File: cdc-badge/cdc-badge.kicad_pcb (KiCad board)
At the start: 4 copper layers, 85 x 110 mm, 158 parts, among them J1 USB_C, J2 JST S2B-PH-SM4-TB, J3 Conn_02x20_Odd_Even, J4 Conn_Grove, J5 Conn_02x03_Odd_Even, J6 Conn_01x06, J7 Conn_01x24, Q1 Si1308EDL, Q2 Si1308EDL, SW0 0, SW1 1, SW10 YES, SW11 NO, SW12 power on/reset, SW13 reset, SW14 flash/power off, SW15 MST-22D18G2 3J, SW16 MST-22D18G2 3J, SW17 MS-22D28-G020, SW2 2, SW3 3, SW4 4, SW5 5, SW6 6, SW7 7, SW8 8, SW9 9, U1 ESP32-S3-WROOM-1-N16R8, U2 TCA9535PWR, U3 TR01-C2P-T301, U5 TLV61070ADBVR, U6 BQ25895RTW, U7 USBLC6-2SC6, U8 TLV62569DBV

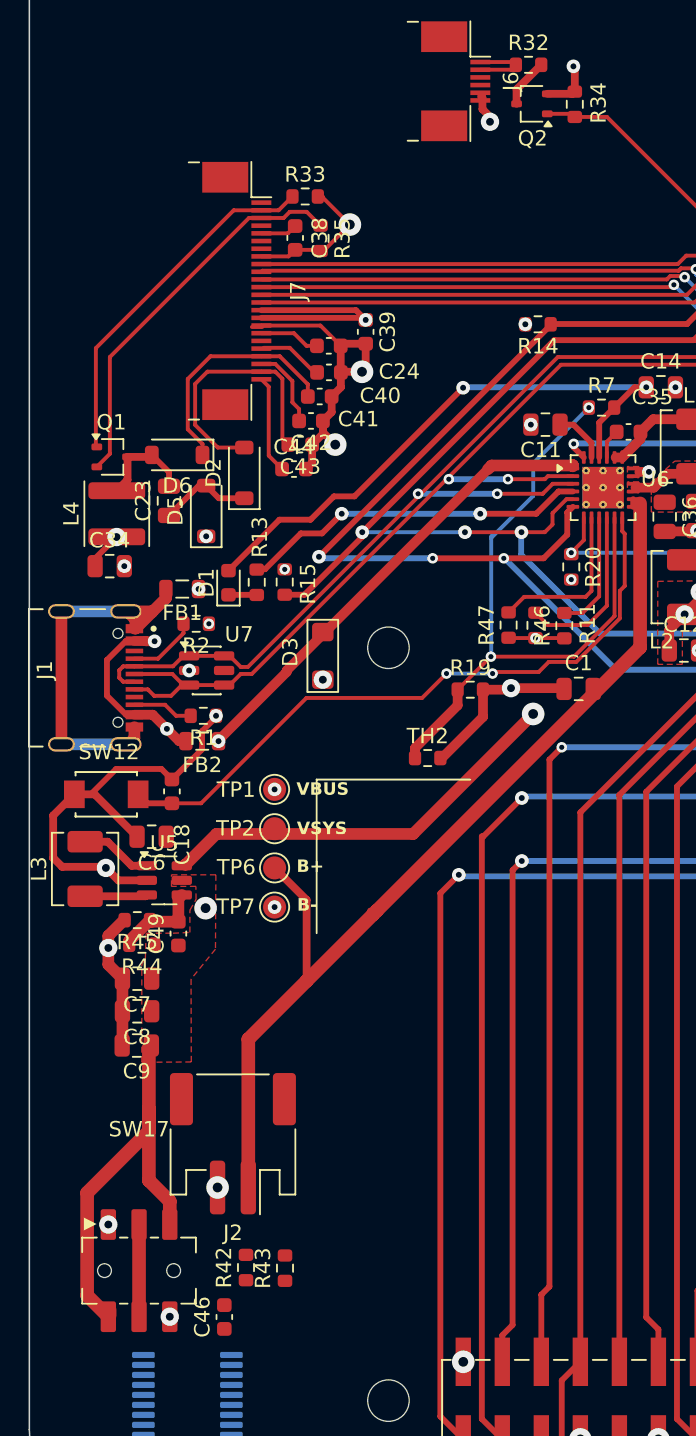
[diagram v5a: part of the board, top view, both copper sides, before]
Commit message: PCB: Reviewed wirings, fixed some errors
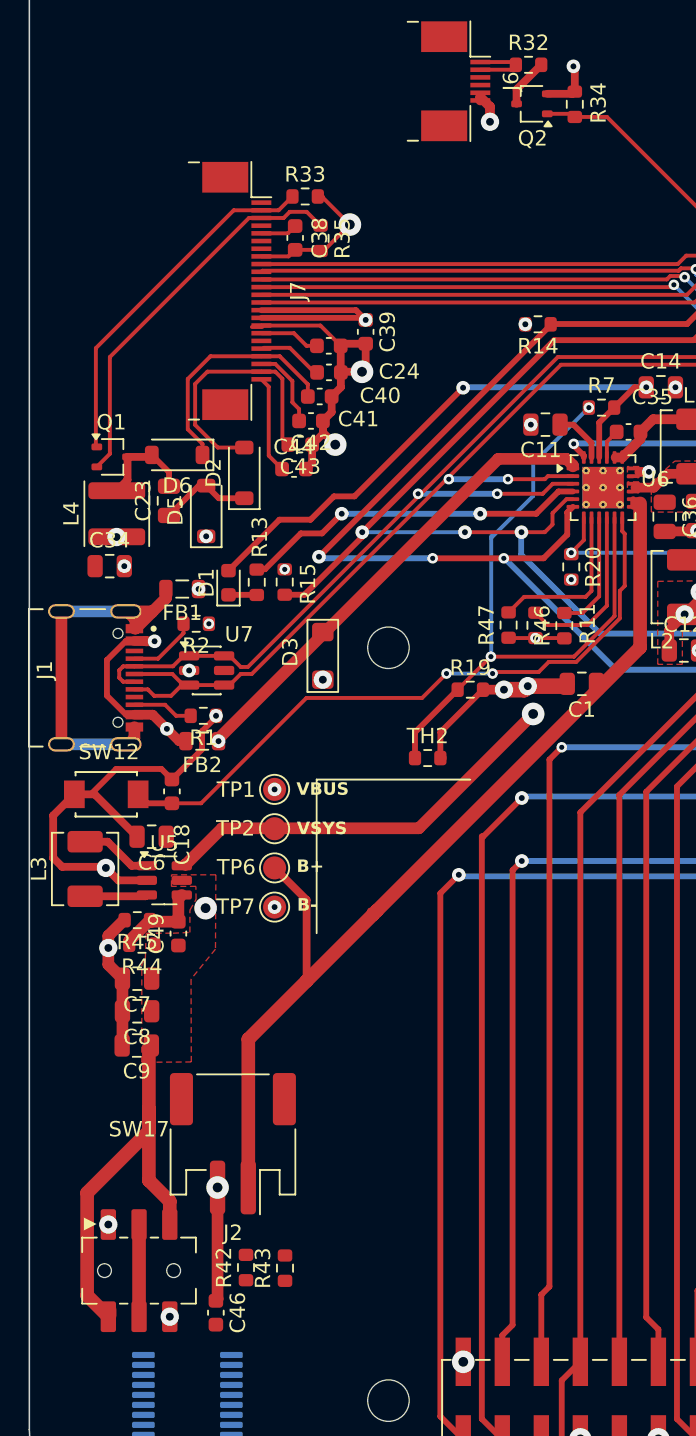
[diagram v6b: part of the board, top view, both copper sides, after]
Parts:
- moved C46 0.62 mm to (35.9, 138.9), turned to -90 degrees
- moved C1 0.39 mm to (59.7, 98.0), turned to 180 degrees
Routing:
- net GND: track 146.4 -> 154.2 mm, vias 44 -> 45
- net +3.3V: track 44.4 -> 43.0 mm

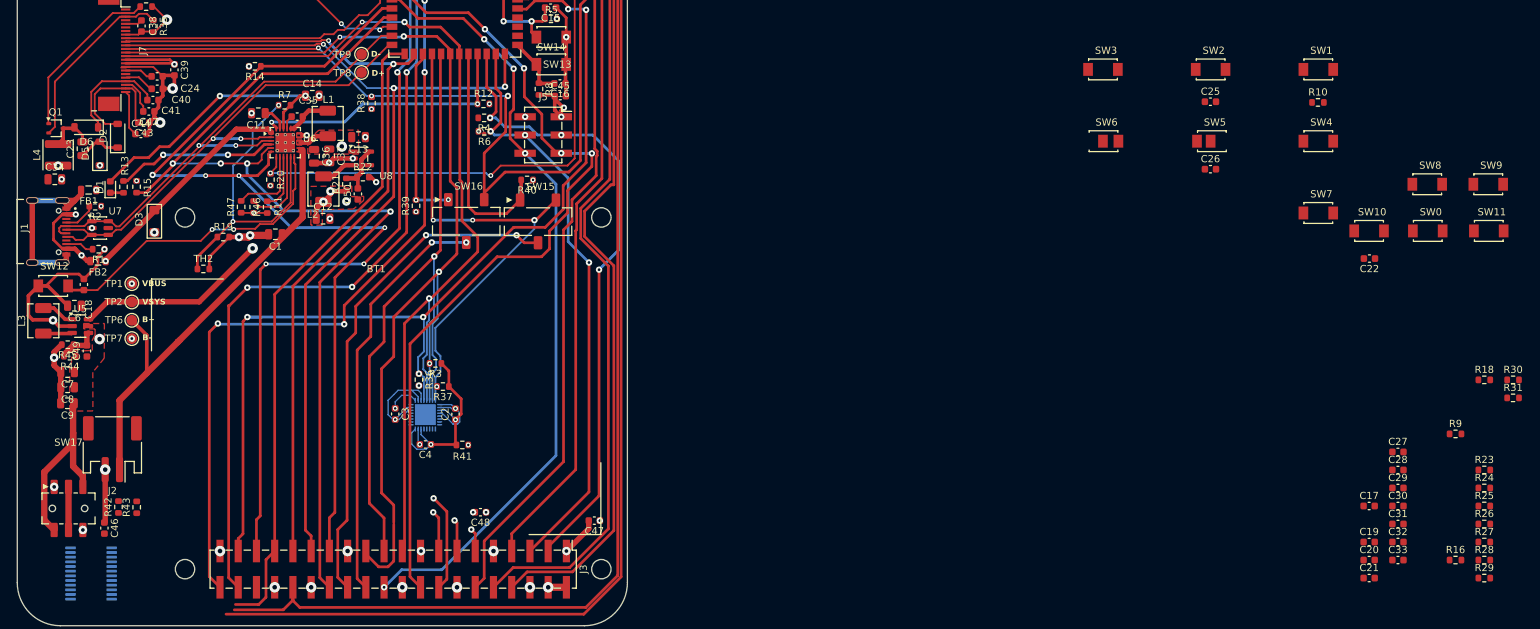
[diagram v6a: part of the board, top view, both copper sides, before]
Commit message: PCB: placement and begin routing for the buttons/keypad
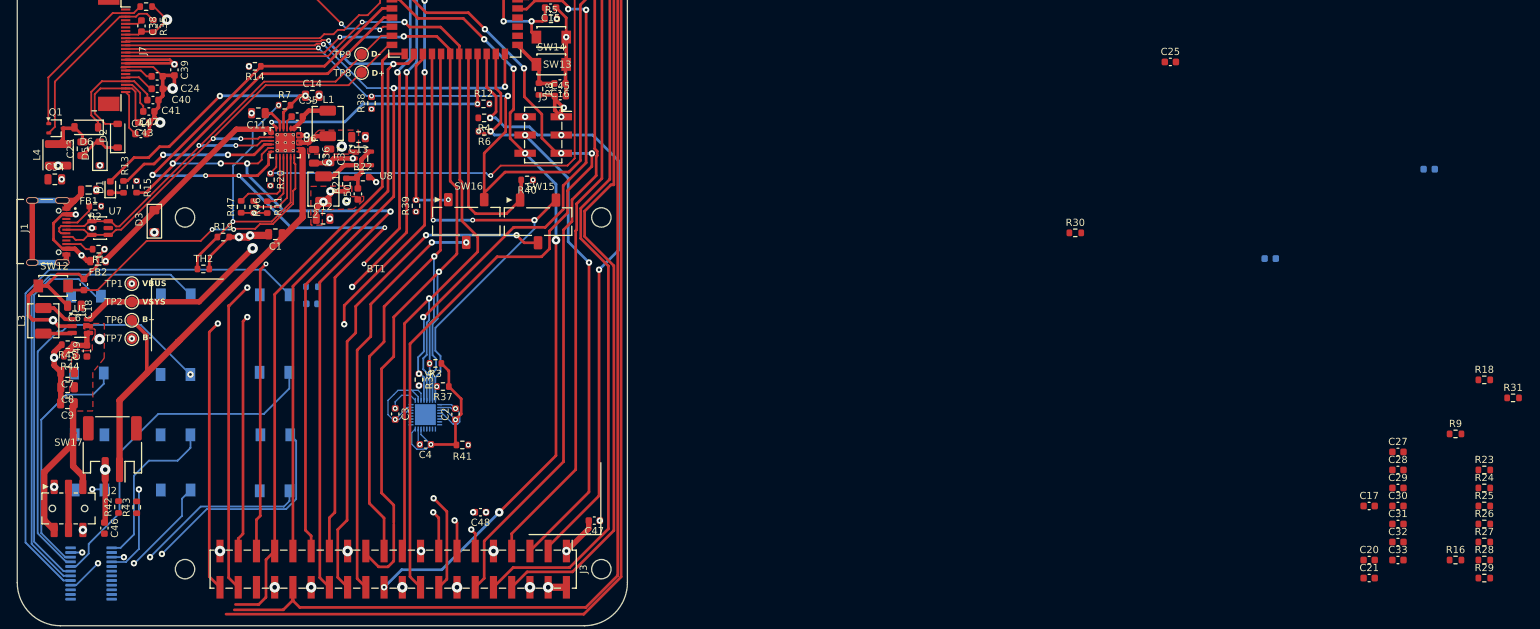
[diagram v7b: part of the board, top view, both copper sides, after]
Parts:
- C19, C22, C26, R10, SW0, SW1, SW10, SW11, SW2, SW3, SW4, SW5, SW6, SW7, SW8, SW9: moved to B.Cu
- moved SW11 198.2 mm to (33.8, 133.6), turned to 180 degrees
- moved SW9 198.0 mm to (33.8, 125.9), turned to 180 degrees
- moved SW0 178.1 mm to (45.8, 133.6), turned to 180 degrees
- moved SW8 177.8 mm to (45.8, 125.9), turned to 180 degrees
- moved SW10 156.7 mm to (59.6, 133.7), turned to 180 degrees
- moved C19 151.0 mm to (64.8, 107.7), turned to 180 degrees
- moved SW4 148.9 mm to (59.6, 117.2), turned to 180 degrees
- moved SW1 148.7 mm to (59.6, 106.4), turned to 180 degrees
- moved SW7 148.5 mm to (59.7, 125.9), turned to 180 degrees
- moved SW5 148.0 mm to (45.8, 117.5), turned to 180 degrees
- moved SW2 147.5 mm to (45.8, 106.4), turned to 180 degrees
- moved SW3 145.2 mm to (33.3, 106.6), turned to 180 degrees
- moved SW6 145.0 mm to (33.7, 117.3), turned to 180 degrees
- moved R10 142.5 mm to (64.8, 105.3), turned to 180 degrees
- moved R30 64.3 mm to (171.1, 97.8)
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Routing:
- net /BTN_1: track 0.00 -> 82.8 mm
- net /BTN_2: track 0.00 -> 66.5 mm
- net /BTN_5: track 0.00 -> 57.2 mm, vias 0 -> 1
- net /BTN_3: track 0.00 -> 52.4 mm
- net /BTN_4: track 0.00 -> 49.1 mm
- net /BTN_7: track 0.00 -> 44.7 mm, vias 0 -> 2
- net /BTN_6: track 0.00 -> 33.5 mm
- net /BTN_YES: track 0.00 -> 29.4 mm, vias 0 -> 2
- net /BTN_0: track 0.00 -> 23.6 mm, vias 0 -> 2
- net /BTN_8: track 0.00 -> 23.4 mm
- net /BTN_NO: track 0.00 -> 21.1 mm, vias 0 -> 2
- net /TR01_IRQ: track 137.7 -> 135.7 mm
- net /SAO_GPIO2: vias 4 -> 6

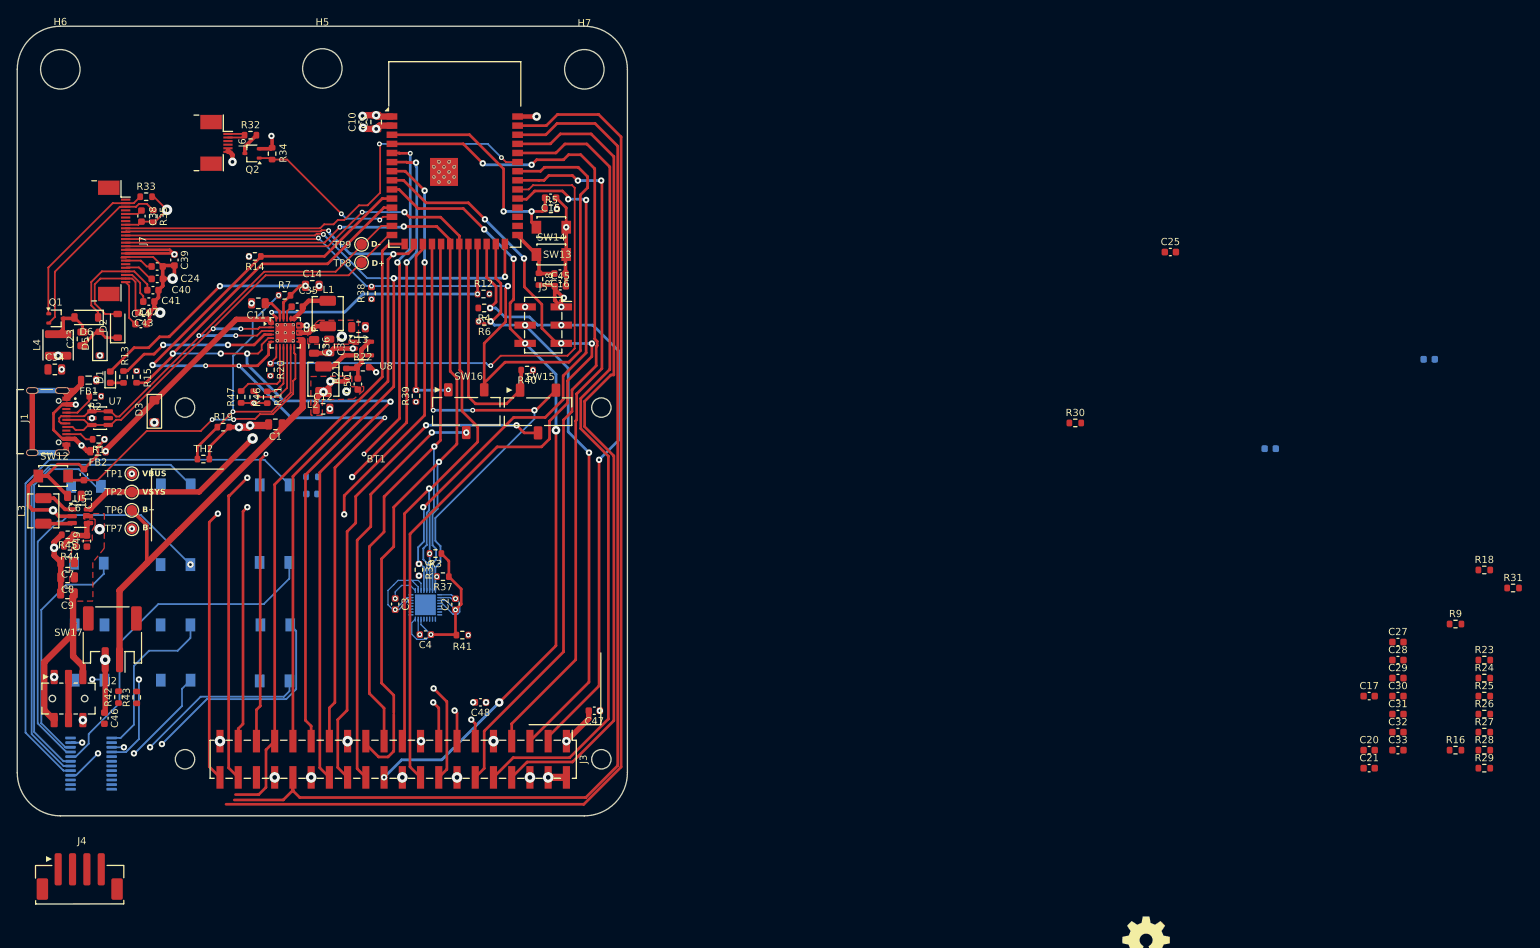
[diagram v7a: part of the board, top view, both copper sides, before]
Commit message: PCB: Erased all Components and tracks for full redesign
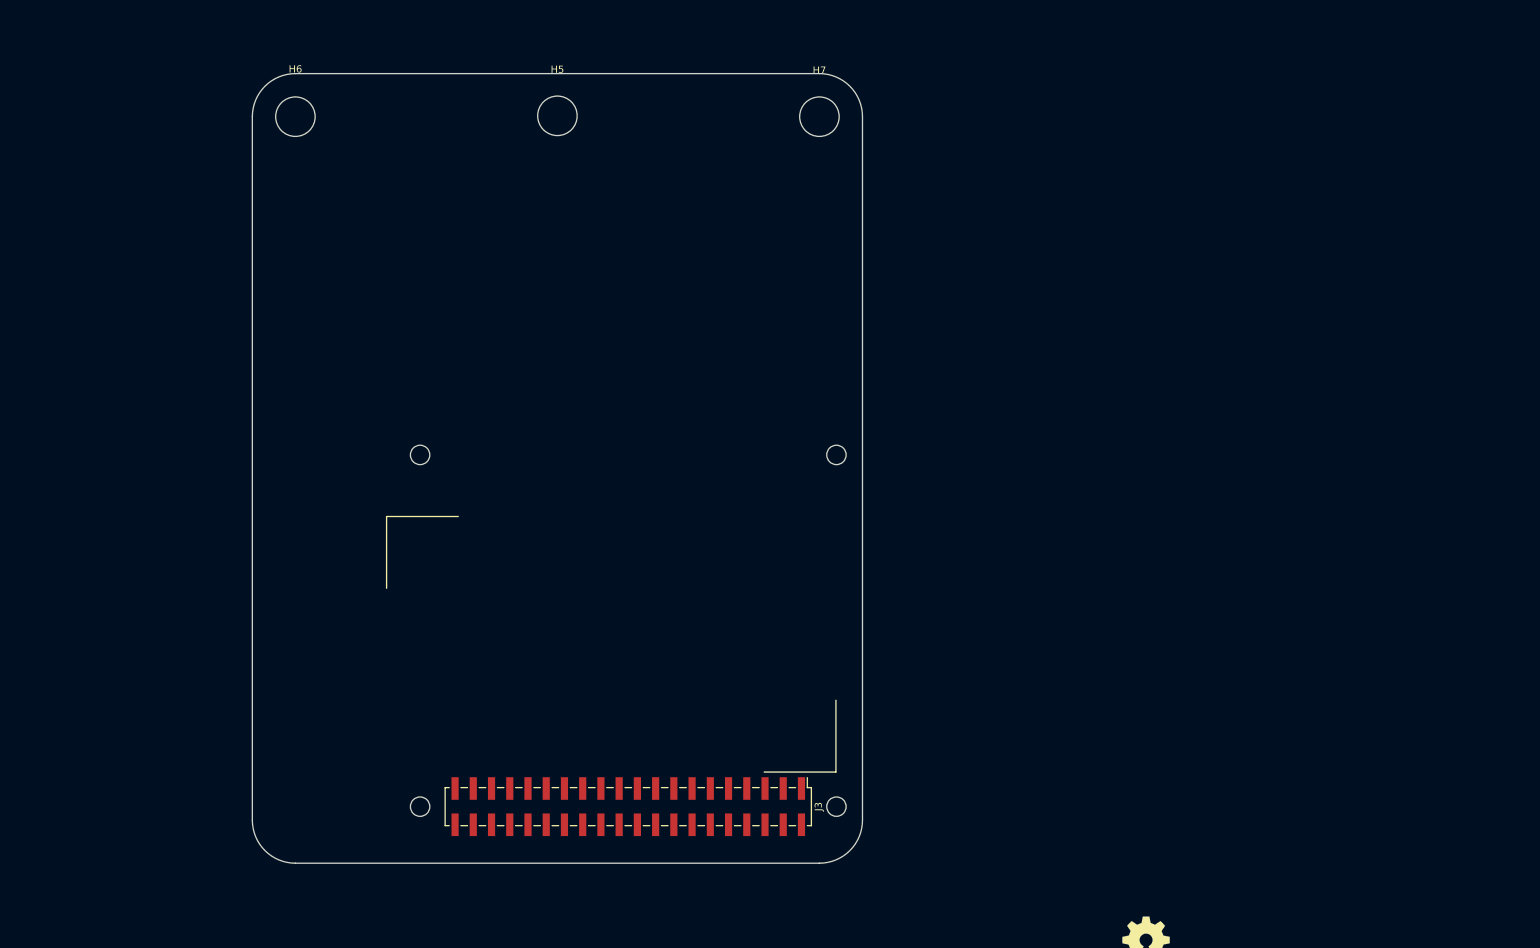
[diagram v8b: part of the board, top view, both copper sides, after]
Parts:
- removed C1, C11, C12, C36, C37, C5, C6, C7, C8, C9: 10uF, Capacitor_SMD:C_0805_2012Metric
- removed C10, C15, C16, C17, C18, C19, C2, C20, C21, C22, C25, C26, C27, C28, C29, C3, C30, C31, C32, C4: 100nF, Capacitor_SMD:C_0603_1608Metric
- removed C13, C14, C23, C34: 4.7uF, Capacitor_SMD:C_0805_2012Metric
- removed C24, C33, C38, C39, C40, C41, C42, C43, C44, C45, C46, C47, C48: 1uF, Capacitor_SMD:C_0603_1608Metric
- removed C35: 47nF, Capacitor_SMD:C_0603_1608Metric
- removed C49, C50: NA, Capacitor_SMD:C_0603_1608Metric
- removed D1: red, LED_SMD:LED_0603_1608Metric
- removed D2, D5, D6: MBR0530, Diode_SMD:D_SOD-123
- removed D3: SMF14CA, CDC_Badge:D_SOD-123FL_Unpolarized
- removed DS1: GDEY029T94-FL03, CDC_Badge:GDEY029T94-FL03
- removed FB1: 30Ω@100MHz, Inductor_SMD:L_0805_2012Metric
- removed FB2: 120Ω@100MHz, Inductor_SMD:L_0805_2012Metric
- removed J1: USB_C, CDC_Badge:SHOUHAN_TYPE-C_16PIN_2MD_073
- removed J2: JST S2B-PH-SM4-TB, Connector_JST:JST_PH_S2B-PH-SM4-TB_1x02-1MP_P2.00mm_Horizontal
- removed J4: Conn_Grove, CDC_Badge:BOOMELE_HY-4P_1x04-1MP_P2mm_Vertical
- removed J5: Conn_02x03_Odd_Even, Connector_PinSocket_2.54mm:PinSocket_2x03_P2.54mm_Vertical_SMD
- removed J6: Conn_01x06, Connector_FFC-FPC:Jushuo_AFC07-S06FCA-00_1x6-1MP_P0.50_Horizontal
- removed J7: Conn_01x24, Connector_FFC-FPC:Jushuo_AFC07-S24FCA-00_1x24-1MP_P0.50_Horizontal
- removed L1, L2, L3: 2.2uH, Inductor_SMD:L_TechFuse_SL0420
- removed L4: 47uH, Inductor_SMD:L_Changjiang_FNR4030S
- removed Q1, Q2: Si1308EDL, Package_TO_SOT_SMD:SOT-323_SC-70
- removed R1, R13, R2, R7: 5.1k, Resistor_SMD:R_0603_1608Metric
- removed R10, R16, R18, R23, R24, R25, R26, R27, R28, R29, R3, R30, R31, R36, R37, R38, R39, R40: 47k, Resistor_SMD:R_0603_1608Metric
- removed R11: 220, Resistor_SMD:R_0603_1608Metric
- removed R12, R14, R15, R20, R4, R42, R43, R46, R47, R5, R6, R8, R9, TH2: 10k, Resistor_SMD:R_0603_1608Metric
- removed R19, R22: 30k, Resistor_SMD:R_0603_1608Metric
- removed R21: 135k, Resistor_SMD:R_0603_1608Metric
- removed R32: 5.1, Resistor_SMD:R_0603_1608Metric
- removed R33, R34: 1M, Resistor_SMD:R_0603_1608Metric
- removed R35: 2.2, Resistor_SMD:R_0603_1608Metric
- removed R41: 0, Resistor_SMD:R_0603_1608Metric
- removed R44: 820k, Resistor_SMD:R_0603_1608Metric
- removed R45: 91k, Resistor_SMD:R_0603_1608Metric
- removed SW0: 0, CDC_Badge:TS-1088-AR02016
- removed SW1: 1, CDC_Badge:TS-1088-AR02016
- removed SW10: YES, CDC_Badge:TS-1088-AR02016
- removed SW11: NO, CDC_Badge:TS-1088-AR02016
- removed SW12: power on/reset, CDC_Badge:TS-1088-AR02016
- removed SW13: reset, CDC_Badge:TS-1088-AR02016
- removed SW14: flash/power off, CDC_Badge:TS-1088-AR02016
- removed SW15, SW16: MST-22D18G2 3J, CDC_Badge:SW_SPDT_Shouhan_MST-22D18G2_3J
- removed SW17: MS-22D28-G020, CDC_Badge:SW_DPDT_G-Switch_MS-22D28-G020
- removed SW2: 2, CDC_Badge:TS-1088-AR02016
- removed SW3: 3, CDC_Badge:TS-1088-AR02016
- removed SW4: 4, CDC_Badge:TS-1088-AR02016
- removed SW5: 5, CDC_Badge:TS-1088-AR02016
- removed SW6: 6, CDC_Badge:TS-1088-AR02016
- removed SW7: 7, CDC_Badge:TS-1088-AR02016
- removed SW8: 8, CDC_Badge:TS-1088-AR02016
- removed SW9: 9, CDC_Badge:TS-1088-AR02016
- removed TP1: TP_VBUS, TestPoint:TestPoint_Pad_D1.5mm
- removed TP2: TP_VSYS, TestPoint:TestPoint_Pad_D1.5mm
- removed TP6: TP_BAT+, TestPoint:TestPoint_Pad_D1.5mm
- removed TP7: TP_BAT-, TestPoint:TestPoint_Pad_D1.5mm
- removed TP8: TP_USB_D+, TestPoint:TestPoint_Pad_D1.5mm
- removed TP9: TP_USB_D-, TestPoint:TestPoint_Pad_D1.5mm
- removed U1: ESP32-S3-WROOM-1-N16R8, CDC_Badge:ESP32-S3-WROOM-1
- removed U2: TCA9535PWR, Package_SO:TSSOP-24_4.4x7.8mm_P0.65mm
- removed U3: TR01-C2P-T301, Package_DFN_QFN:QFN-32-1EP_4x4mm_P0.4mm_EP2.9x2.9mm
- removed U5: TLV61070ADBVR, Package_TO_SOT_SMD:SOT-23-6
- removed U6: BQ25895RTW, Package_DFN_QFN:Texas_RTW_WQFN-24-1EP_4x4mm_P0.5mm_EP2.7x2.7mm_ThermalVias
- removed U7: USBLC6-2SC6, Package_TO_SOT_SMD:SOT-23-6
- removed U8: TLV62569DBV, Package_TO_SOT_SMD:SOT-23-5
- moved BT1 33.4 mm to (106.5, 128.6)
- moved H1 33.4 mm to (79.9, 102.2)
- moved H2 33.4 mm to (137.9, 102.2)
- moved H3 33.4 mm to (79.9, 151.2)
- moved H4 33.4 mm to (137.9, 151.2)
- moved H5 33.4 mm to (99.0, 55.0)
- moved H6 33.4 mm to (62.5, 55.1)
- moved H7 33.4 mm to (135.5, 55.1)
- moved J3 33.4 mm to (108.9, 151.2)
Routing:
- net /GROVE0: track 162.1 -> 0.00 mm
- net /EXP_IRQ: track 161.3 -> 0.00 mm
- net GND: track 154.2 -> 0.00 mm, vias 45 -> 0
- net /SPI_SCLK: track 147.9 -> 0.00 mm, vias 3 -> 0
- net /I2C0_SCL: track 142.1 -> 0.00 mm, vias 4 -> 0
- net /SPI_MOSI: track 140.6 -> 0.00 mm, vias 3 -> 0
- net /TR01_IRQ: track 135.7 -> 0.00 mm, vias 5 -> 0
- net /I2C0_SDA: track 133.3 -> 0.00 mm, vias 4 -> 0
- net /SPI_DC_EPD: track 130.1 -> 0.00 mm, vias 3 -> 0
- net /SPI_CS_EPD: track 123.3 -> 0.00 mm, vias 3 -> 0
- net /PCM_CLK: track 122.8 -> 0.00 mm, vias 2 -> 0
- net /SAO_GPIO1: track 116.6 -> 0.00 mm, vias 4 -> 0
- net /SPI_RST_EPD: track 116.3 -> 0.00 mm, vias 2 -> 0
- net /TXD: track 115.0 -> 0.00 mm
- net /RXD: track 114.3 -> 0.00 mm
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- removed copper zone on F.Cu, net +3.3V
- removed copper zone on In2.Cu, net +3.3V
- removed copper zone on F.Cu, net +5V
- removed copper zone on F.Cu, net GND
- removed copper zone on In1.Cu, net GND
- removed copper zone on F.Cu, net VSYS
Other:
- board text removed: "B+"
- board text removed: "B-"
- board text removed: "D+"
- board text removed: "D-"
- board text removed: "VBUS"
- board text removed: "VSYS"
